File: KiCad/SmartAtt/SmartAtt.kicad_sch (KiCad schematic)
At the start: 44 parts, among them IC1 74LVC4245APW,112, J1 RF_base, J2 RF_base_gnd, J3 12V, J4 UART_FW, J5 RF_mine, J6 RF_mine_gnd, U1 MP-N, U2 AMS1117-3.3, U3 ESP32-WROOM-32E, U4 HMC542BLP4ETR, U5 OLED

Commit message: ...
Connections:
- net GND: now also U4.25 (GND_T_pad)
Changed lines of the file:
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@@
 	)
 	(junction
+		(at 30.48 45.72)
+		(diameter 0)
+		(color 0 0 0 0)
+	)
+	(junction
 		(at 39.37 43.18)
 		(diameter 0)
@@
 	)
 	(junction
+		(at 110.49 156.21)
+		(diameter 0)
+		(color 0 0 0 0)
+	)
+	(junction
 		(at 194.31 35.56)
 		(diameter 0)
@@
 	)
 	(junction
+		(at 36.83 40.64)
+		(diameter 0)
+		(color 0 0 0 0)
+	)
+	(junction
 		(at 186.69 40.64)
 		(diameter 0)
@@
 	(wire
 		(pts
+			(xy 125.73 138.43) (xy 99.06 138.43)
+		)
+		(stroke
+			(width 0)
+			(type default)
+		)
+	)
+	(wire
+		(pts
 			(xy 118.11 140.97) (xy 110.49 140.97)
 		)
@@
 	(wire
 		(pts
+			(xy 99.06 156.21) (xy 110.49 156.21)
+		)
+		(stroke
+			(width 0)
+			(type default)
+		)
+	)
+	(wire
+		(pts
 			(xy 196.85 124.46) (xy 179.07 124.46)
 		)
@@
 	(wire
 		(pts
+			(xy 125.73 142.24) (xy 125.73 138.43)
+		)
+		(stroke
+			(width 0)
+			(type default)
+		)
+	)
+	(wire
+		(pts
 			(xy 151.13 33.02) (xy 162.56 33.02)
 		)
@@
 	(wire
 		(pts
+			(xy 30.48 45.72) (xy 30.48 43.18)
+		)
+		(stroke
+			(width 0)
+			(type default)
+		)
+	)
+	(wire
+		(pts
 			(xy 128.27 167.64) (xy 138.43 167.64)
 		)
@@
 	(wire
 		(pts
-			(xy 30.48 100.33) (xy 30.48 43.18)
+			(xy 30.48 100.33) (xy 30.48 45.72)
 		)
 		(stroke
@@
 	(wire
 		(pts
-			(xy 36.83 39.37) (xy 36.83 45.72)
+			(xy 36.83 39.37) (xy 36.83 40.64)
 		)
 		(stroke
@@
 	(wire
 		(pts
+			(xy 128.27 142.24) (xy 125.73 142.24)
+		)
+		(stroke
+			(width 0)
+			(type default)
+		)
+	)
+	(wire
+		(pts
 			(xy 41.91 43.18) (xy 39.37 43.18)
 		)
@@
 	(wire
 		(pts
+			(xy 36.83 40.64) (xy 36.83 45.72)
+		)
+		(stroke
+			(width 0)
+			(type default)
+		)
+	)
+	(wire
+		(pts
 			(xy 260.35 128.27) (xy 260.35 130.81)
 		)
@@
 	(wire
 		(pts
+			(xy 99.06 138.43) (xy 99.06 156.21)
+		)
+		(stroke
+			(width 0)
+			(type default)
+		)
+	)
+	(wire
+		(pts
 			(xy 140.97 167.64) (xy 143.51 167.64)
 		)
@@
 	)
 	(symbol
+		(lib_id "power:PWR_FLAG")
+		(at 30.48 45.72 90)
+		(unit 1)
+		(exclude_from_sim no)
+		(in_bom yes)
+		(on_board yes)
+		(dnp no)
+		(fields_autoplaced yes)
+		(property "Reference" "#FLG02"
+			(at 28.575 45.72 0)
+			(effects
+				(font
+					(size 1.27 1.27)
+				)
+				(hide yes)
+			)
+		)
+		(property "Value" "PWR_FLAG"
+			(at 26.67 45.7199 90)
+			(effects
+				(font
+					(size 1.27 1.27)
+				)
+				(justify left)
+			)
+		)
+		(property "Footprint" ""
+			(at 30.48 45.72 0)
+			(effects
+				(font
+					(size 1.27 1.27)
+				)
+				(hide yes)
+			)
+		)
+		(property "Datasheet" "~"
+			(at 30.48 45.72 0)
+			(effects
+				(font
+					(size 1.27 1.27)
+				)
+				(hide yes)
+			)
+		)
+		(property "Description" "Special symbol for telling ERC where power comes from"
+			(at 30.48 45.72 0)
+			(effects
+				(font
+					(size 1.27 1.27)
+				)
+				(hide yes)
+			)
+		)
+		(pin "1"
+		)
+		(instances
+			(project "SmartAtt"
+				(path "/51c17e9b-7dab-4c11-afbb-666453ecee80"
+					(reference "#FLG02")
+					(unit 1)
+				)
+			)
+		)
+	)
+	(symbol
 		(lib_id "Device:R")
 		(at 143.51 25.4 90)
@@
 	)
 	(symbol
+		(lib_id "power:PWR_FLAG")
+		(at 36.83 40.64 90)
+		(unit 1)
+		(exclude_from_sim no)
+		(in_bom yes)
+		(on_board yes)
+		(dnp no)
+		(fields_autoplaced yes)
+		(property "Reference" "#FLG01"
+			(at 34.925 40.64 0)
+			(effects
+				(font
+					(size 1.27 1.27)
+				)
+				(hide yes)
+			)
+		)
+		(property "Value" "PWR_FLAG"
+			(at 33.02 40.6399 90)
+			(effects
+				(font
+					(size 1.27 1.27)
+				)
+				(justify left)
+			)
+		)
+		(property "Footprint" ""
+			(at 36.83 40.64 0)
+			(effects
+				(font
+					(size 1.27 1.27)
+				)
+				(hide yes)
+			)
+		)
+		(property "Datasheet" "~"
+			(at 36.83 40.64 0)
+			(effects
+				(font
+					(size 1.27 1.27)
+				)
+				(hide yes)
+			)
+		)
+		(property "Description" "Special symbol for telling ERC where power comes from"
+			(at 36.83 40.64 0)
+			(effects
+				(font
+					(size 1.27 1.27)
+				)
+				(hide yes)
+			)
+		)
+		(pin "1"
+		)
+		(instances
+			(project "SmartAtt"
+				(path "/51c17e9b-7dab-4c11-afbb-666453ecee80"
+					(reference "#FLG01")
+					(unit 1)
+				)
+			)
+		)
+	)
+	(symbol
 		(lib_id "power:GND")
 		(at 248.92 44.45 0)
@@
 		(pin "19"
 		)
+		(pin "25"
+		)
 		(instances

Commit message: pochti zakonchil razvodku
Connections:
- net +5V: now also C6.1, U4.2 (Vcc)
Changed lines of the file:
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@@
 	)
 	(junction
+		(at 110.49 140.97)
+		(diameter 0)
+		(color 0 0 0 0)
+	)
+	(junction
 		(at 58.42 44.45)
 		(diameter 0)
@@
 	(wire
 		(pts
+			(xy 110.49 133.35) (xy 110.49 140.97)
+		)
+		(stroke
+			(width 0)
+			(type default)
+		)
+	)
+	(wire
+		(pts
 			(xy 137.16 119.38) (xy 137.16 124.46)
 		)
@@
 					(unit 1)
 				)
+			)
+		)
+	)
+	(symbol
+		(lib_id "power:+5V")
+		(at 110.49 133.35 0)
+		(unit 1)
+		(exclude_from_sim no)
+		(in_bom yes)
+		(on_board yes)
+		(dnp no)
+		(fields_autoplaced yes)
+		(property "Reference" "#PWR033"
+			(at 110.49 137.16 0)
+			(effects
+				(font
+					(size 1.27 1.27)
+				)
+				(hide yes)
+			)
+		)
+		(property "Value" "+5V"
+			(at 110.49 128.27 0)
+			(effects
+				(font
+					(size 1.27 1.27)
+				)
+			)
+		)
+		(property "Footprint" ""
+			(at 110.49 133.35 0)
+			(effects
+				(font
+					(size 1.27 1.27)
+				)
+				(hide yes)
+			)
+		)
+		(property "Datasheet" ""
+			(at 110.49 133.35 0)
+			(effects
+				(font
+					(size 1.27 1.27)
+				)
+				(hide yes)
+			)
+		)
+		(property "Description" "Power symbol creates a global label with name \"+5V\""
+			(at 110.49 133.35 0)
+			(effects
+				(font
+					(size 1.27 1.27)
+				)
+				(hide yes)
+			)
+		)
+		(pin "1"
+		)
+		(instances
+			(project "SmartAtt"
+				(path "/51c17e9b-7dab-4c11-afbb-666453ecee80"
+					(reference "#PWR033")
+					(unit 1)
+				)

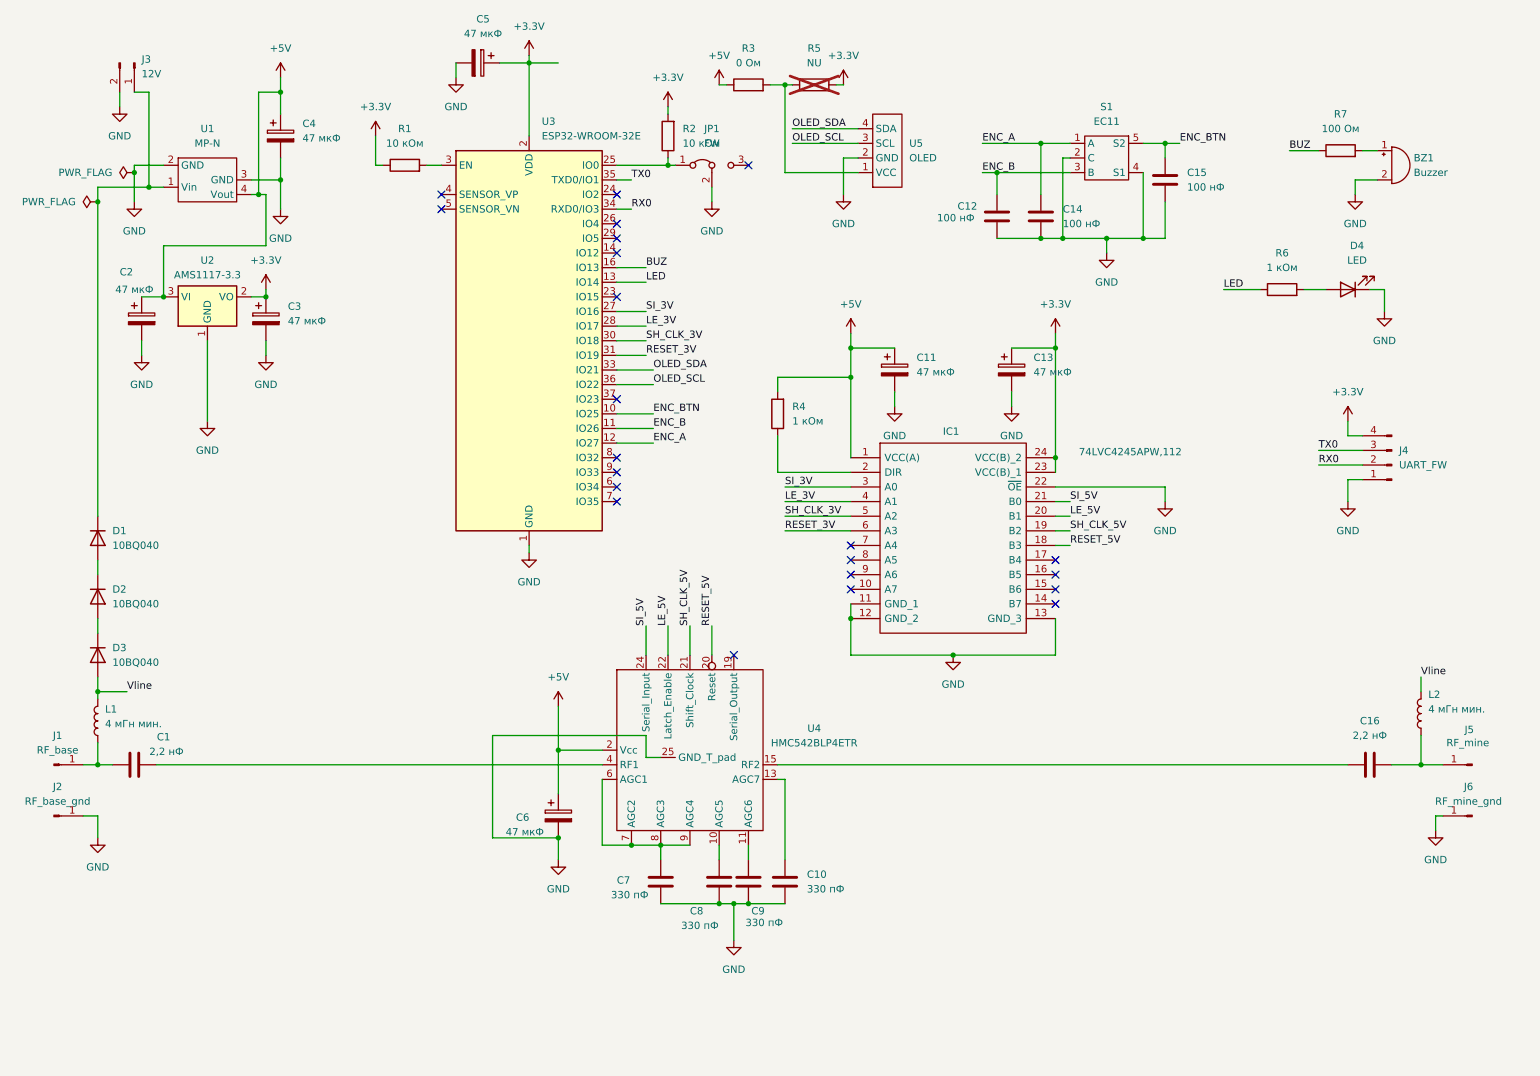
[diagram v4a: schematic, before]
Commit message: fix mpn gnd-5v. fix C 5-10mm
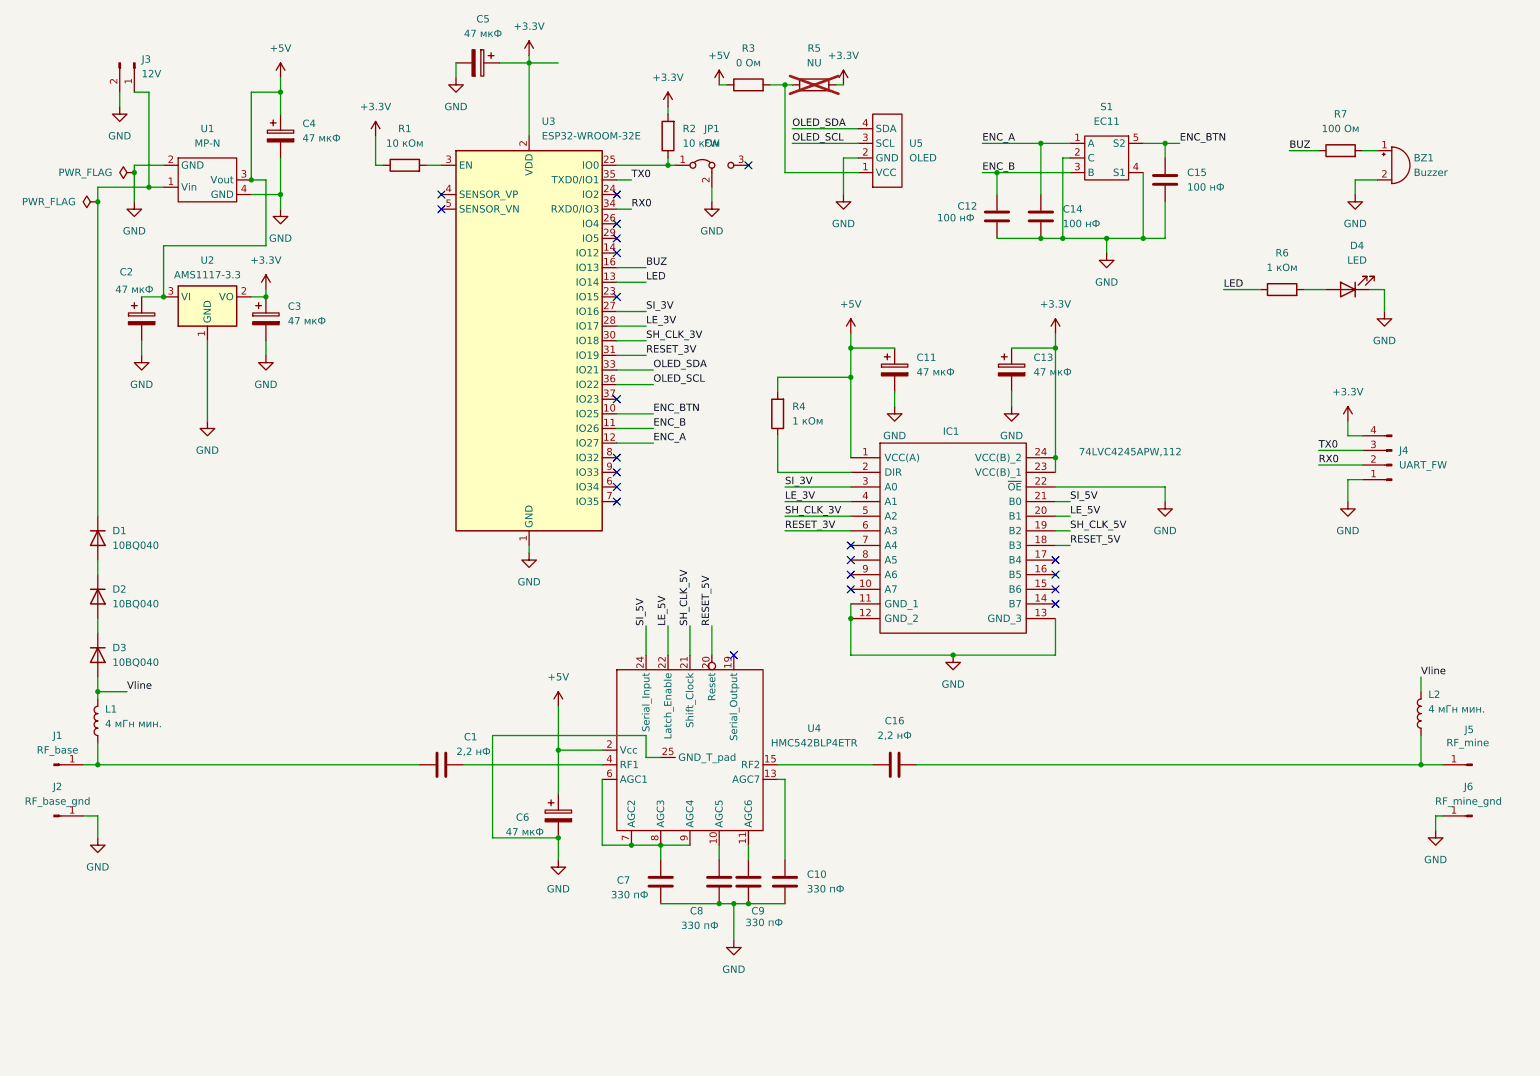
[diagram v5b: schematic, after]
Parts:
- C1, C16: footprint Capacitor_THT:C_Disc_D10.0mm_W2.5mm_P5.00mm -> Capacitor_THT:C_Disc_D7.5mm_W5.0mm_P10.00mm
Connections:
- net +5V: now also U1.3 (Vout); no longer U1.4 (Vout)
- net GND: now also U1.4 (GND); no longer U1.3 (GND)
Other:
- moved on the sheet: C1, C16
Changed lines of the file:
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@@
 	)
 	(junction
+		(at 62.23 44.45)
+		(diameter 0)
+		(color 0 0 0 0)
+	)
+	(junction
 		(at 140.97 167.64)
 		(diameter 0)
@@
 	)
 	(junction
-		(at 58.42 44.45)
-		(diameter 0)
-		(color 0 0 0 0)
-	)
-	(junction
 		(at 149.86 25.4)
 		(diameter 0)
@@
 	)
 	(junction
-		(at 62.23 41.91)
+		(at 196.85 71.12)
 		(diameter 0)
 		(color 0 0 0 0)
 	)
 	(junction
-		(at 196.85 71.12)
+		(at 57.15 41.91)
 		(diameter 0)
 		(color 0 0 0 0)
@@
 	(wire
 		(pts
-			(xy 255.27 143.51) (xy 260.35 143.51)
+			(xy 172.72 143.51) (xy 260.35 143.51)
 		)
 		(stroke
@@
 	(wire
 		(pts
-			(xy 59.69 44.45) (xy 58.42 44.45)
-		)
-		(stroke
-			(width 0)
-			(type default)
-		)
-	)
-	(wire
-		(pts
 			(xy 129.54 38.1) (xy 129.54 39.37)
 		)
@@
 	(wire
 		(pts
-			(xy 62.23 38.1) (xy 62.23 41.91)
+			(xy 62.23 38.1) (xy 62.23 44.45)
 		)
 		(stroke
@@
 	(wire
 		(pts
-			(xy 30.48 143.51) (xy 33.02 143.51)
+			(xy 30.48 143.51) (xy 86.36 143.51)
 		)
 		(stroke
@@
 	(wire
 		(pts
-			(xy 59.69 44.45) (xy 59.69 53.34)
-		)
-		(stroke
-			(width 0)
-			(type default)
-		)
-	)
-	(wire
-		(pts
 			(xy 129.54 29.21) (xy 129.54 30.48)
 		)
@@
 	(wire
 		(pts
+			(xy 59.69 41.91) (xy 57.15 41.91)
+		)
+		(stroke
+			(width 0)
+			(type default)
+		)
+	)
+	(wire
+		(pts
 			(xy 186.69 40.64) (xy 199.39 40.64)
 		)
@@
 	(wire
 		(pts
-			(xy 58.42 26.67) (xy 62.23 26.67)
+			(xy 57.15 41.91) (xy 57.15 26.67)
 		)
 		(stroke
@@
 	(wire
 		(pts
-			(xy 62.23 46.99) (xy 62.23 41.91)
-		)
-		(stroke
-			(width 0)
-			(type default)
-		)
-	)
-	(wire
-		(pts
 			(xy 30.48 128.27) (xy 30.48 130.81)
 		)
@@
 	(wire
 		(pts
+			(xy 57.15 44.45) (xy 62.23 44.45)
+		)
+		(stroke
+			(width 0)
+			(type default)
+		)
+	)
+	(wire
+		(pts
 			(xy 161.29 68.58) (xy 161.29 71.12)
 		)
@@
 	(wire
 		(pts
-			(xy 40.64 143.51) (xy 118.11 143.51)
+			(xy 93.98 143.51) (xy 118.11 143.51)
 		)
 		(stroke
@@
 	(wire
 		(pts
+			(xy 57.15 26.67) (xy 62.23 26.67)
+		)
+		(stroke
+			(width 0)
+			(type default)
+		)
+	)
+	(wire
+		(pts
 			(xy 30.48 118.11) (xy 30.48 120.65)
 		)
@@
 	(wire
 		(pts
+			(xy 62.23 44.45) (xy 62.23 46.99)
+		)
+		(stroke
+			(width 0)
+			(type default)
+		)
+	)
+	(wire
+		(pts
 			(xy 78.74 34.29) (xy 78.74 39.37)
 		)
@@
 	(wire
 		(pts
-			(xy 148.59 143.51) (xy 247.65 143.51)
+			(xy 148.59 143.51) (xy 165.1 143.51)
 		)
 		(stroke
@@
 	(wire
 		(pts
-			(xy 58.42 44.45) (xy 57.15 44.45)
-		)
-		(stroke
-			(width 0)
-			(type default)
-		)
-	)
-	(wire
-		(pts
 			(xy 105.41 20.32) (xy 105.41 21.59)
 		)
@@
 	(wire
 		(pts
-			(xy 58.42 44.45) (xy 58.42 26.67)
-		)
-		(stroke
-			(width 0)
-			(type default)
-		)
-	)
-	(wire
-		(pts
 			(xy 87.63 39.37) (xy 90.17 39.37)
 		)
@@
 	(wire
 		(pts
-			(xy 62.23 41.91) (xy 57.15 41.91)
-		)
-		(stroke
-			(width 0)
-			(type default)
-		)
-	)
-	(wire
-		(pts
 			(xy 38.1 62.23) (xy 41.91 62.23)
 		)
@@
 	(wire
 		(pts
+			(xy 59.69 53.34) (xy 59.69 41.91)
+		)
+		(stroke
+			(width 0)
+			(type default)
+		)
+	)
+	(wire
+		(pts
 			(xy 140.97 167.64) (xy 143.51 167.64)
 		)
@@
 	(symbol
 		(lib_id "Device:C")
-		(at 251.46 143.51 270)
+		(at 168.91 143.51 270)
 		(unit 1)
 		(exclude_from_sim no)
@@
 		(fields_autoplaced yes)
 		(property "Reference" "C16"
-			(at 251.46 135.89 90)
+			(at 168.91 135.89 90)
 			(effects
 				(font
@@
 		)
 		(property "Value" "2,2 нФ"
-			(at 251.46 138.43 90)
+			(at 168.91 138.43 90)
 			(effects
 				(font
@@
 			)
 		)
-		(property "Footprint" "Capacitor_THT:C_Disc_D10.0mm_W2.5mm_P5.00mm"
-			(at 247.65 144.4752 0)
+		(property "Footprint" "Capacitor_THT:C_Disc_D7.5mm_W5.0mm_P10.00mm"
+			(at 165.1 144.4752 0)
 			(effects
 				(font
@@
 		)
 		(property "Datasheet" "~"
-			(at 251.46 143.51 0)
+			(at 168.91 143.51 0)
 			(effects
 				(font
@@
 		)
 		(property "Description" "Unpolarized capacitor"
-			(at 251.46 143.51 0)
+			(at 168.91 143.51 0)
 			(effects
 				(font
@@
 	(symbol
 		(lib_id "Device:C")
-		(at 36.83 143.51 270)
+		(at 90.17 143.51 270)
 		(unit 1)
 		(exclude_from_sim no)
@@
 		(dnp no)
 		(property "Reference" "C1"
-			(at 41.91 138.684 90)
+			(at 95.25 138.684 90)
 			(effects
 				(font
@@
 		)
 		(property "Value" "2,2 нФ"
-			(at 42.418 141.224 90)
+			(at 95.758 141.224 90)
 			(effects
 				(font
@@
 			)
 		)
-		(property "Footprint" "Capacitor_THT:C_Disc_D10.0mm_W2.5mm_P5.00mm"
-			(at 33.02 144.4752 0)
+		(property "Footprint" "Capacitor_THT:C_Disc_D7.5mm_W5.0mm_P10.00mm"
+			(at 86.36 144.4752 0)
 			(effects
 				(font
@@
 		)
 		(property "Datasheet" "~"
-			(at 36.83 143.51 0)
+			(at 90.17 143.51 0)
 			(effects
 				(font
@@
 		)
 		(property "Description" "Unpolarized capacitor"
-			(at 36.83 143.51 0)
+			(at 90.17 143.51 0)
 			(effects
 				(font
